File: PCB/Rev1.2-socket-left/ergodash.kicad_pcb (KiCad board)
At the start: 2 copper layers, 149.9 x 127.4 mm, 83 parts, among them J1 5PIN, SW1 SW_PUSH, SW10 SW_PUSH, SW11 SW_PUSH, SW12 SW_PUSH, SW13 SW_PUSH, SW14 SW_PUSH, SW15 SW_PUSH, SW16 SW_PUSH, SW17 SW_PUSH, SW18 SW_PUSH, SW19 SW_PUSH, SW2 SW_PUSH, SW20 SW_PUSH, SW21 SW_PUSH, SW22 SW_PUSH, SW23 SW_PUSH, SW24 SW_PUSH, SW25 SW_PUSH, SW26 SW_PUSH, SW27 SW_PUSH, SW28 SW_PUSH, SW29 SW_Push, SW3 SW_PUSH, SW30 SW_PUSH, SW31 SW_PUSH, SW32 SW_PUSH, SW33 SW_PUSH, SW34 SW_PUSH, SW35 SW_PUSH, SW4 SW_PUSH, SW40 SW_PUSH, SW5 SW_PUSH, SW6 SW_PUSH, SW7 SW_PUSH, SW8 SW_PUSH, SW9 SW_PUSH, U1 HOLE, U2 HOLE, U3 ProMicro, U4 HOLE, U5 HOLE, U7 HOLE, U8 HOLE, U9 HOLE

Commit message: Remove vestigial U6, add Pro Micro pin labels, refresh both boards
Schematic cleanup: delete U6 (the right-hand Pro Micro left over from the
original reversible design) from both halves' schematics. It was on_board=no
so it never appeared in the netlist or on the board; removing it just drops
dead symbols. Both schematics remain electrically identical.

Left board: add silkscreen pin-name labels (RAW/GND/RST/VCC/TX0/RX1...) around
the Pro Micro, and stamp the title block as Socket-left.

Right board: re-mirror from the left so it inherits the new pin labels and is
stamped Socket-right (mirror_right.py now swaps the title). Regenerate gerbers
and drill for both halves.

DRC: left 130 / right 131 violations (all pre-existing cosmetic/library items,
down from 137), schematic-parity 0, unrouted 0.

Co-Authored-By: Claude Opus 4.8 <noreply@anthropic.com>
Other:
- board text added: "GND"
- board text added: "RAW"
- board text added: "RST"
- board text added: "RX1"
- board text added: "TX0"
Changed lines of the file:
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@@
 	(paper "A4")
 	(title_block
-		(title "ErgoDash Rev2")
-		(date "2018-06-07")
-		(rev "2.0")
-		(company "Omkbd")
+		(title "ErgoDash Rev2 Socket-left")
+		(date "2026-06-13")
+		(rev "2.1")
+		(company "tsubu")
 	)
 	(layers
@@
 		(layer "Edge.Cuts")
 	)
+	(gr_text "RX1"
+		(at 131.978 42.256 0)
+		(layer "F.SilkS")
+		(effects
+			(font
+				(size 1 1)
+				(thickness 0.15)
+			)
+			(justify left bottom)
+		)
+	)
+	(gr_text "GND"
+		(at 131.978 44.756 0)
+		(layer "F.SilkS")
+		(effects
+			(font
+				(size 1 1)
+				(thickness 0.15)
+			)
+			(justify left bottom)
+		)
+	)
+	(gr_text "TX0"
+		(at 132.478 39.756 0)
+		(layer "F.SilkS")
+		(effects
+			(font
+				(size 1 1)
+				(thickness 0.15)
+			)
+			(justify left bottom)
+		)
+	)
+	(gr_text "RAW"
+		(at 152.978 39.756 0)
+		(layer "F.SilkS")
+		(effects
+			(font
+				(size 1 1)
+				(thickness 0.15)
+			)
+			(justify left bottom)
+		)
+	)
+	(gr_text "GND"
+		(at 152.978 42.256 0)
+		(layer "F.SilkS")
+		(effects
+			(font
+				(size 1 1)
+				(thickness 0.15)
+			)
+			(justify left bottom)
+		)
+	)
+	(gr_text "RST"
+		(at 152.978 45.256 0)
+		(layer "F.SilkS")
+		(effects
+			(font
+				(size 1 1)
+				(thickness 0.15)
+			)
+			(justify left bottom)
+		)
+	)
 	(gr_text "ErgoDash Rev. 1.2\nSocketed by tsubu"
 		(at 151.638 139.7 0)
@@
 		)
 	)
+	(gr_text "TX0"
+		(at 134.978 39.756 0)
+		(layer "B.SilkS")
+		(effects
+			(font
+				(size 1 1)
+				(thickness 0.15)
+			)
+			(justify left bottom mirror)
+		)
+	)
+	(gr_text "RX1"
+		(at 134.978 42.256 0)
+		(layer "B.SilkS")
+		(effects
+			(font
+				(size 1 1)
+				(thickness 0.15)
+			)
+			(justify left bottom mirror)
+		)
+	)
+	(gr_text "GND"
+		(at 134.978 44.756 0)
+		(layer "B.SilkS")
+		(effects
+			(font
+				(size 1 1)
+				(thickness 0.15)
+			)
+			(justify left bottom mirror)
+		)
+	)
+	(gr_text "RST"
+		(at 155.978 45.256 0)
+		(layer "B.SilkS")
+		(effects
+			(font
+				(size 1 1)
+				(thickness 0.15)
+			)
+			(justify left bottom mirror)
+		)
+	)
+	(gr_text "RAW"
+		(at 156.478 39.756 0)
+		(layer "B.SilkS")
+		(effects
+			(font
+				(size 1 1)
+				(thickness 0.15)
+			)
+			(justify left bottom mirror)
+		)
+	)
+	(gr_text "GND"
+		(at 156.478 42.256 0)
+		(layer "B.SilkS")
+		(effects
+			(font
+				(size 1 1)
+				(thickness 0.15)
+			)
+			(justify left bottom mirror)
+		)
+	)

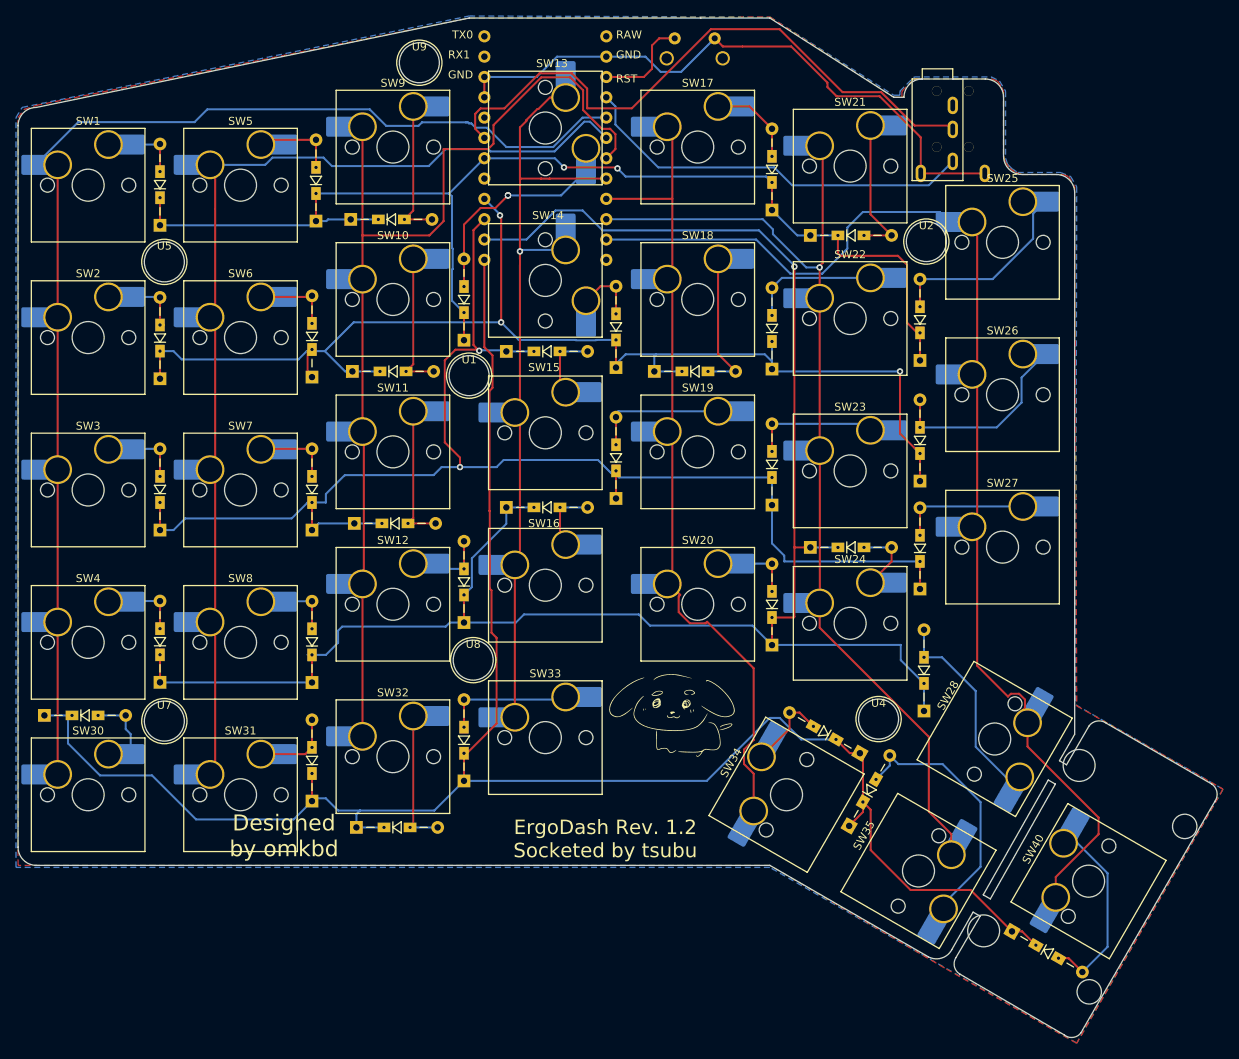
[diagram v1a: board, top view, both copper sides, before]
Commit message: WIP: flip left-board sockets to front (geometry only)
Stage 1 of the socket-on-front re-layout (Option B). Every keyswitch/socket
footprint is flipped in place via flip_sockets_front.py so the Kailh socket SMD
pads now mount on F.Cu and the switch through-holes move to the back-insertion
(left-right mirrored) MX pattern.

This intentionally leaves the matrix DISCONNECTED (71 unconnected items): the old
traces fed the B.Cu socket pads / old hole positions. Matrix rerouting is the
next stage, done by hand in KiCad.

Co-Authored-By: Claude Opus 4.8 <noreply@anthropic.com>
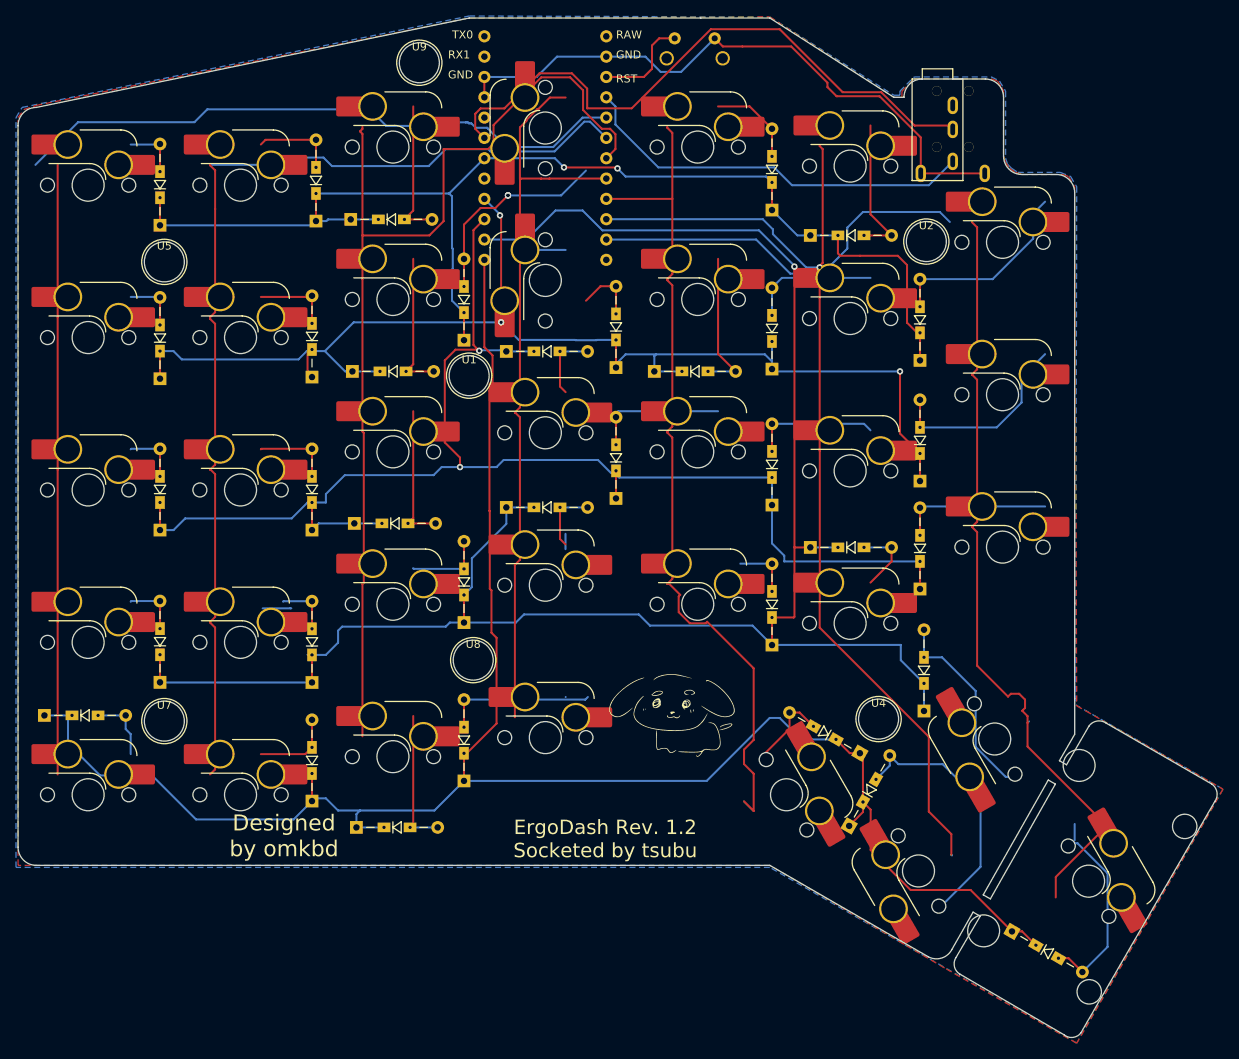
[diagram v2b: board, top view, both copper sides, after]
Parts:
- SW1, SW10, SW11, SW12, SW13, SW14, SW15, SW16, SW17, SW18, SW19, SW2, SW20, SW21, SW22, SW23, SW24, SW25, SW26, SW27, SW28, SW3, SW30, SW31, SW32, SW33, SW34, SW35, SW4, SW40, SW5, SW6, SW7, SW8, SW9: moved to B.Cu
- turned SW1 to 180 degrees
- turned SW10 to 180 degrees
- turned SW11 to 180 degrees
- turned SW12 to 180 degrees
- turned SW15 to 180 degrees
- turned SW16 to 180 degrees
- turned SW17 to 180 degrees
- turned SW18 to 180 degrees
- turned SW19 to 180 degrees
- turned SW2 to 180 degrees
- turned SW20 to 180 degrees
- turned SW21 to 180 degrees
- turned SW22 to 180 degrees
- turned SW23 to 180 degrees
- turned SW24 to 180 degrees
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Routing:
- net Net-(D8-A): track 10.7 -> 7.09 mm
- net /col1: track 132.6 -> 136.2 mm

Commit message: Rotate SW35/SW40 so flipped sockets sit on the board
After flipping the sockets to the front, the SMD socket pads of two edge thumb
keys overhung the board outline (DRC copper_edge_clearance 0.0 mm). Rotate them
back onto the board, folded into flip_sockets_front.py for reproducibility:
  - SW40 (2U): +180 deg only (90 would make it a vertical 2U)
  - SW35 (1U square): +270 deg

Board now has zero copper_edge_clearance violations. Matrix still unrouted
(69 unconnected) -- routing is the next stage.

Co-Authored-By: Claude Opus 4.8 <noreply@anthropic.com>
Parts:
- turned SW35 to -150 degrees
- turned SW40 to -60 degrees
